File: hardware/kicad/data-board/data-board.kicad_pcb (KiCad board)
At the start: 4 copper layers, 120 x 90 mm, 144 parts, among them J1 3.3V LoRaWAN, J14 Conn_02x05_Odd_Even, J17 Molex 470531000, J2 3.3V SWARM, J3 BMS I2C, J4 5V, J5 USB_67298-4090, J6 12V, J7 USB_OTG, J8 Conn_01x04, SW1 Wake, U1 TPD4EUSB30, U10 RAK5146, U11 EMC2301-1-ACZL-TR, U12 Swarm_M138, U13 FSUSB42MUX, U14 74LVC1G07SE-7, U2 TPD4EUSB30, U3 MagJack-A70-112-331N126, U4 TPD4EUSB30, U5 74LVC1G07SE-7, U6 USB2514B_Bi, U7 AP2553W6, U8 PCF85063AT/AAZ, U9 74LVC1G07SE-7, Y1 24MHz, Y2 X32K768S301

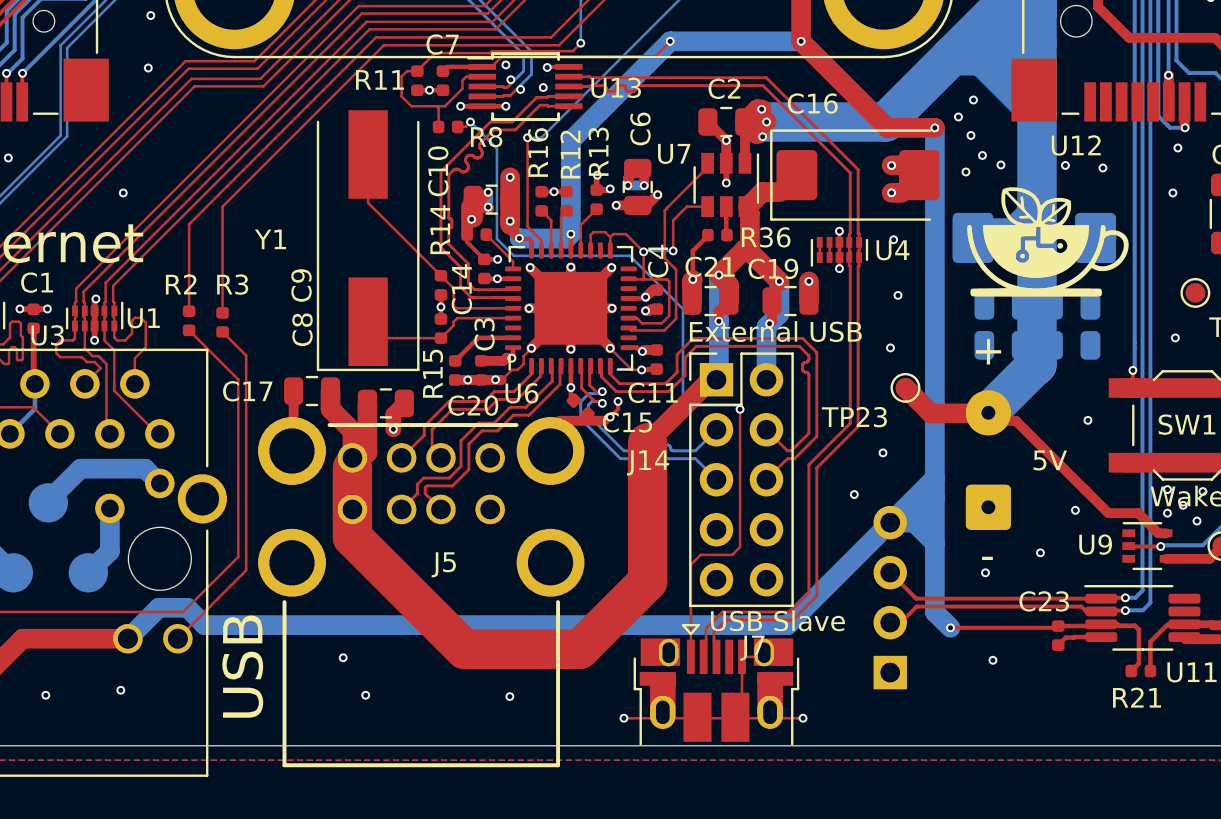
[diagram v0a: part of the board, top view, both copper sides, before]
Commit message: change i2c pin interface
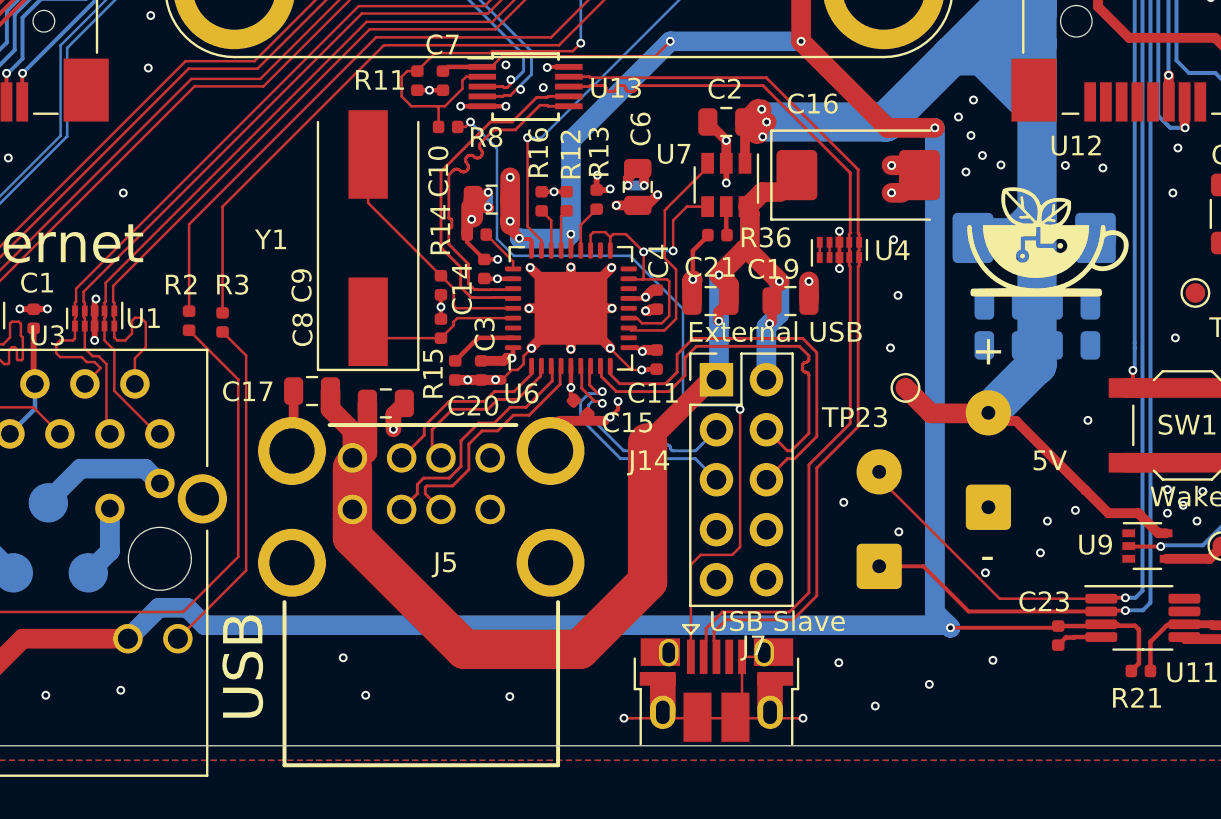
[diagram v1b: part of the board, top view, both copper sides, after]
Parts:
- J3: value BMS I2C -> Power Controller; footprint Connector_PinHeader_2.54mm:PinHeader_1x04_P2.54mm_Vertical -> Teapot:PogoPinContact_2_P4.8mm_D2.3mm_H0.7mm
- moved J3 7.79 mm to (161.1, 135.8), turned to 90 degrees
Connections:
- J3 pad 1: GND -> /SCL1
- J3 pad 2: /SCL1 -> /SDA1
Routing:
- net /+3.3v: track 319.1 -> 312.5 mm
- net /SDA1: track 200.7 -> 203.5 mm
- net /SCL1: track 202.6 -> 203.6 mm
- net GND: vias 306 -> 310

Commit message: add text revision 2.0
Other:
- board text added: "Revision 2"
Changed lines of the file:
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@@
   (gr_arc (start 201.58 57.22) (mid 204.054874 58.245126) (end 205.08 60.72) (layer "Edge.Cuts") (width 0.05))
   (gr_arc (start 205.08 143.72) (mid 204.054874 146.194874) (end 201.58 147.22) (layer "Edge.Cuts") (width 0.05))
+  (gr_text "Revision 2" (at 172.64 143.9) (layer "B.SilkS")
+    (effects (font (size 2 2) (thickness 0.25)) (justify mirror))
+  )
   (gr_text "RAK5146 LoRaWAN\nConcentrator" (at 106.03 86.985) (layer "F.SilkS")
     (effects (font (size 2 2) (thickness 0.3)))
